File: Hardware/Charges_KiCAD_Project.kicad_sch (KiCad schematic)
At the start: 9 parts, among them J1 Terminal Block, J2 Terminal Block

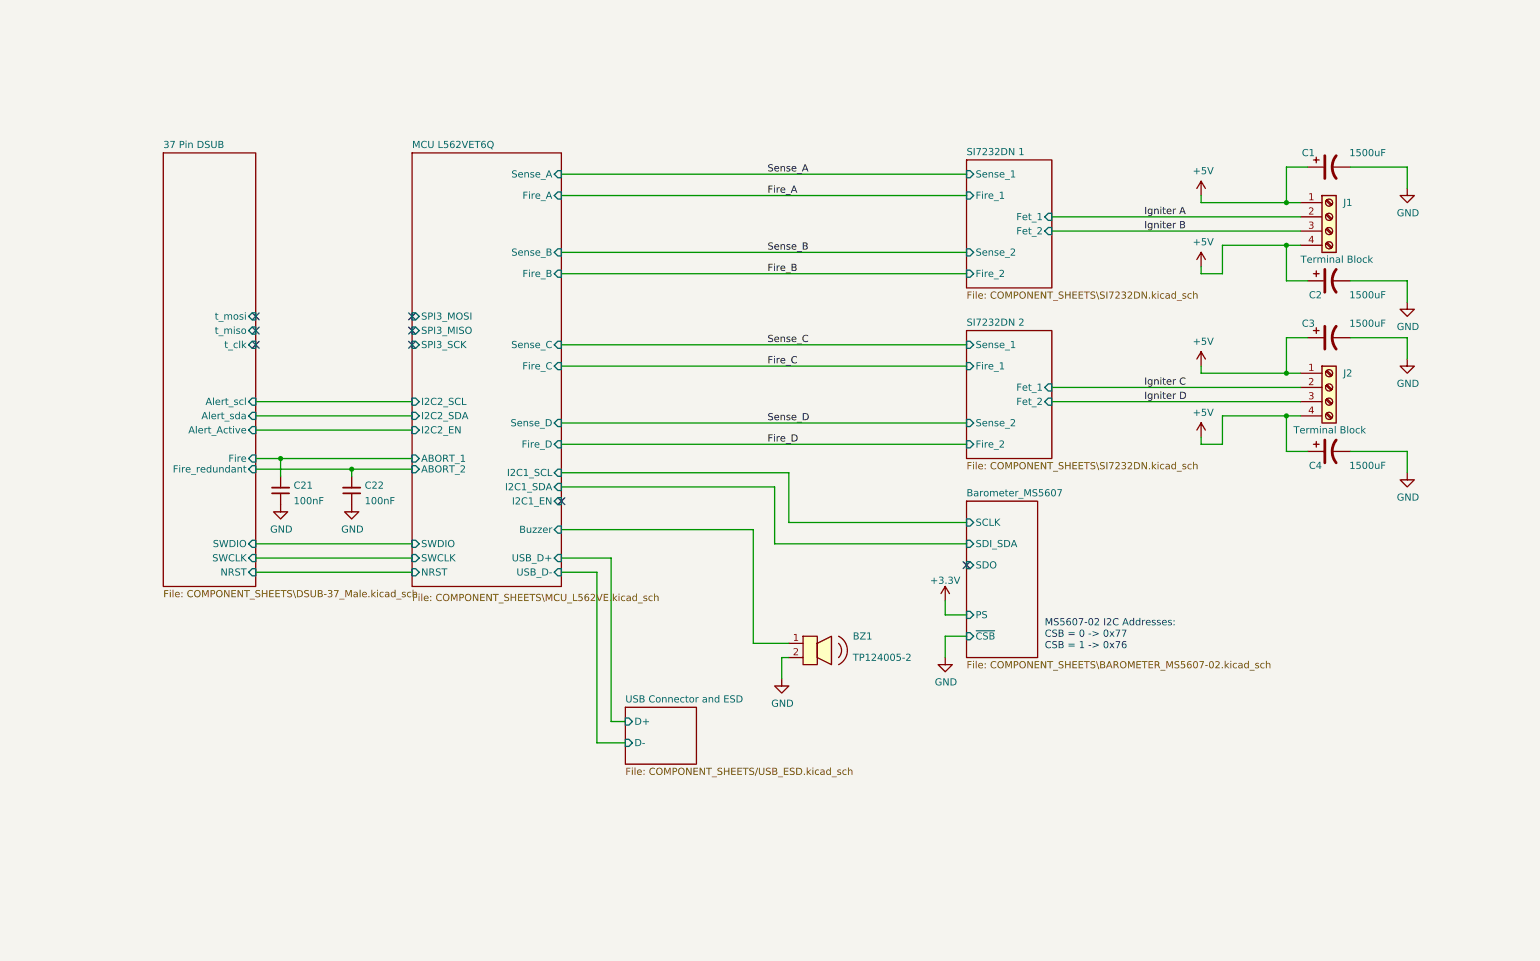
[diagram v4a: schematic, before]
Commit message: Added bleed off resistors to charge capacitors
R = -t/C*ln(V/Vo) = (-1)/(0.0015)*ln(1v/5v) = 1072.96 ≈ 1000 ohm
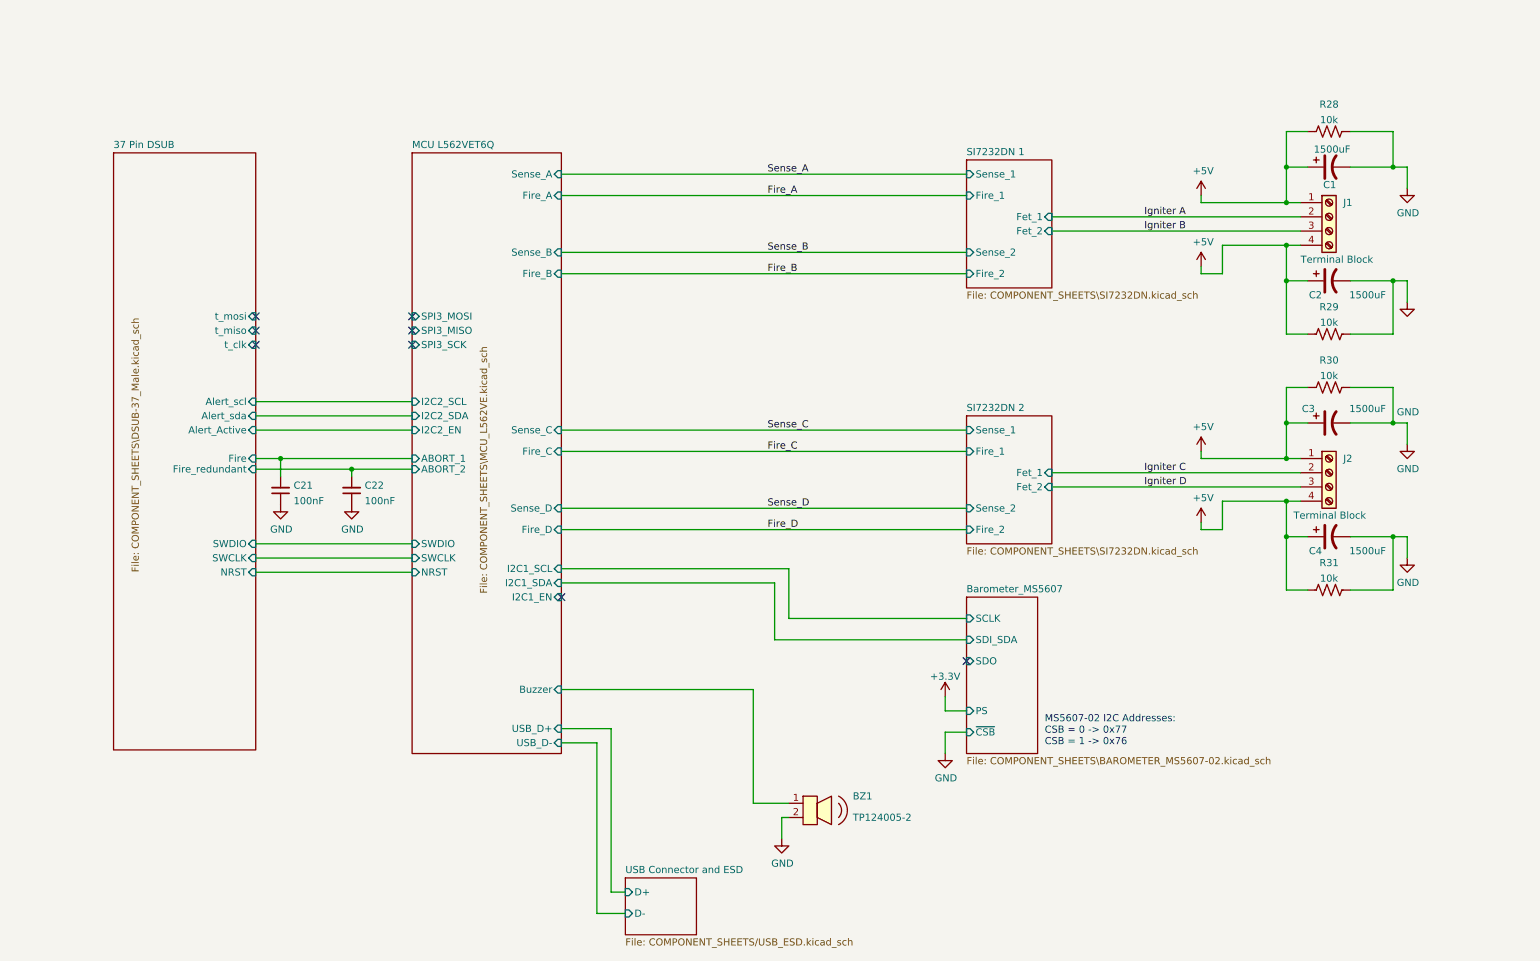
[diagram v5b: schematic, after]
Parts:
- added R28, R29, R30, R31: 10k, Resistor_SMD:R_0603_1608Metric_Pad0.98x0.95mm_HandSolder, symbol Device:R_US
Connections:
- net +5V: now also R28.1, R29.1, R30.1, R31.1
- net GND: now also R28.2, R29.2, R30.2, R31.2
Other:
- moved on the sheet: BZ1, C3, C4, J2
